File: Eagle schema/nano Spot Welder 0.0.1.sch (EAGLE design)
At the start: 37 parts, among them Q1 BC548, Q3 BD137, T1 BTA 41 / 600V, U1 NANO, U2 DISPLAY-NOKIA-5110, U3 DS18B20, X3 ~230V, X4 Mikro trafó

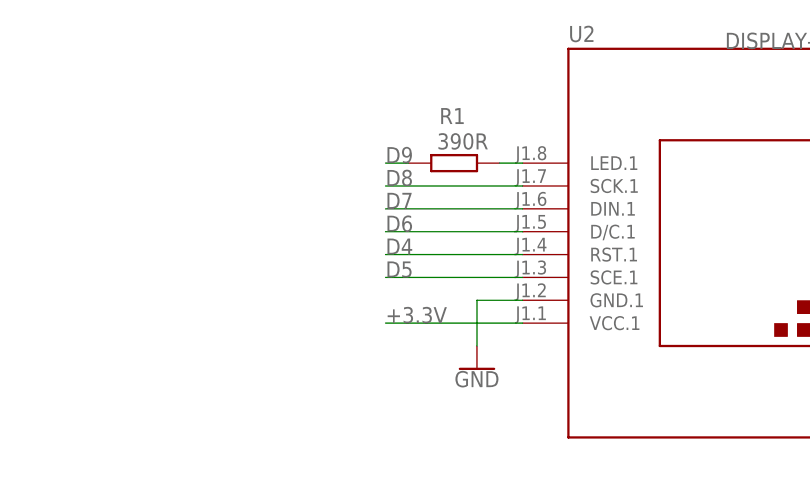
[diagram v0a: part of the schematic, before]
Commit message: - LCD szintillesztő ellenállások - LCD bias & Contrast
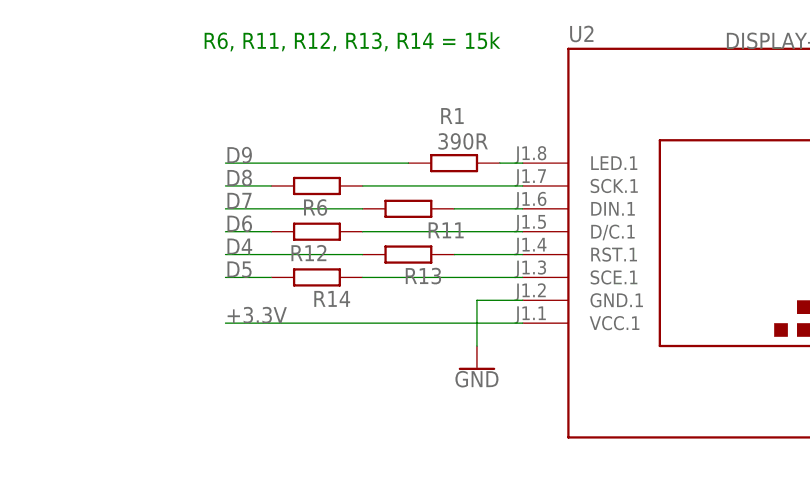
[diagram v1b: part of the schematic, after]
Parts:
- added R11, R12, R13, R14, R6: (no value), resistor:R-EU_0204/7
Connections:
- new net N$10: R12.1, U2.D/C.1
- new net N$11: R13.1, U2.RST.1
- new net N$12: R14.1, U2.SCE.1
- new net N$8: R6.1, U2.SCK.1
- new net N$9: R11.1, U2.DIN.1
- net D4: now also R13.2; no longer U2.RST.1
- net D5: now also R14.2; no longer U2.SCE.1
- net D6: now also R12.2; no longer U2.D/C.1
- net D7: now also R11.2; no longer U2.DIN.1
- net D8: now also R6.2; no longer U2.SCK.1
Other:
- note added: "R6, R11, R12, R13, R14 = 15k"
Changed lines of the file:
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@@
 <layer number="125" name="_tNames" color="7" fill="1" visible="yes" active="yes"/>
 <layer number="126" name="_bNames" color="7" fill="1" visible="yes" active="yes"/>
-<layer number="127" name="_tValues" color="7" fill="1" visible="yes" active="yes"/>
-<layer number="128" name="_bValues" color="7" fill="1" visible="yes" active="yes"/>
+<layer number="127" name="_tValues" color="7" fill="1" visible="no" active="yes"/>
+<layer number="128" name="_bValues" color="7" fill="1" visible="no" active="yes"/>
 <layer number="129" name="Mask" color="7" fill="1" visible="yes" active="yes"/>
 <layer number="130" name="SMDSTROOK" color="7" fill="1" visible="yes" active="yes"/>
@@
 <part name="GND9" library="SparkFun-PowerSymbols" library_urn="urn:adsk.eagle:library:530" deviceset="GND" device=""/>
 <part name="R5" library="resistor" library_urn="urn:adsk.eagle:library:348" deviceset="R-EU_" device="0204/7" package3d_urn="urn:adsk.eagle:package:25945/1" value="56kk"/>
+<part name="R6" library="resistor" library_urn="urn:adsk.eagle:library:348" deviceset="R-EU_" device="0204/7" package3d_urn="urn:adsk.eagle:package:25945/1">
+<attribute name="SPICEPREFIX" value="R"/>
+</part>
+<part name="R11" library="resistor" library_urn="urn:adsk.eagle:library:348" deviceset="R-EU_" device="0204/7" package3d_urn="urn:adsk.eagle:package:25945/1"/>
+<part name="R12" library="resistor" library_urn="urn:adsk.eagle:library:348" deviceset="R-EU_" device="0204/7" package3d_urn="urn:adsk.eagle:package:25945/1"/>
+<part name="R13" library="resistor" library_urn="urn:adsk.eagle:library:348" deviceset="R-EU_" device="0204/7" package3d_urn="urn:adsk.eagle:package:25945/1"/>
+<part name="R14" library="resistor" library_urn="urn:adsk.eagle:library:348" deviceset="R-EU_" device="0204/7" package3d_urn="urn:adsk.eagle:package:25945/1"/>
 </parts>
 <sheets>
@@
 <text x="81.28" y="68.58" size="1.778" layer="91">SW</text>
 <text x="81.28" y="66.04" size="1.778" layer="91">DT</text>
+<text x="50.8" y="129.54" size="1.778" layer="91">R6, R11, R12, R13, R14 = 15k</text>
 </plain>
 <instances>
@@
 <attribute name="NAME" x="1.4986" y="-21.59" size="1.778" layer="95" rot="R270"/>
 <attribute name="VALUE" x="-3.302" y="-21.59" size="1.778" layer="96" rot="R270"/>
+</instance>
+<instance part="R6" gate="G$1" x="63.5" y="114.3" smashed="yes" rot="R180">
+<attribute name="NAME" x="64.77" y="112.8014" size="1.778" layer="95" rot="R180"/>
+<attribute name="VALUE" x="67.31" y="117.602" size="1.778" layer="96" rot="R180"/>
+</instance>
+<instance part="R11" gate="G$1" x="73.66" y="111.76" smashed="yes" rot="R180">
+<attribute name="NAME" x="80.01" y="110.2614" size="1.778" layer="95" rot="R180"/>
+<attribute name="VALUE" x="77.47" y="115.062" size="1.778" layer="96" rot="R180"/>
+</instance>
+<instance part="R12" gate="G$1" x="63.5" y="109.22" smashed="yes" rot="R180">
+<attribute name="NAME" x="64.77" y="107.7214" size="1.778" layer="95" rot="R180"/>
+<attribute name="VALUE" x="67.31" y="112.522" size="1.778" layer="96" rot="R180"/>
+</instance>
+<instance part="R13" gate="G$1" x="73.66" y="106.68" smashed="yes" rot="R180">
+<attribute name="NAME" x="77.47" y="105.1814" size="1.778" layer="95" rot="R180"/>
+<attribute name="VALUE" x="77.47" y="109.982" size="1.778" layer="96" rot="R180"/>
+</instance>
+<instance part="R14" gate="G$1" x="63.5" y="104.14" smashed="yes" rot="R180">
+<attribute name="NAME" x="67.31" y="102.6414" size="1.778" layer="95" rot="R180"/>
+<attribute name="VALUE" x="67.31" y="107.442" size="1.778" layer="96" rot="R180"/>
 </instance>
 </instances>
@@
 <segment>
 <pinref part="U2" gate="G$1" pin="VCC.1"/>
-<wire x1="86.36" y1="99.06" x2="71.12" y2="99.06" width="0.1524" layer="91"/>
-<label x="71.12" y="99.06" size="1.778" layer="95"/>
+<wire x1="86.36" y1="99.06" x2="53.34" y2="99.06" width="0.1524" layer="91"/>
+<label x="53.34" y="99.06" size="1.778" layer="95"/>
 </segment>
 <segment>
@@
 <segment>
 <pinref part="R1" gate="G$1" pin="2"/>
-<wire x1="73.66" y1="116.84" x2="71.12" y2="116.84" width="0.1524" layer="91"/>
-<label x="71.12" y="116.84" size="1.778" layer="95"/>
+<wire x1="73.66" y1="116.84" x2="53.34" y2="116.84" width="0.1524" layer="91"/>
+<label x="53.34" y="116.84" size="1.778" layer="95"/>
 </segment>
 <segment>
@@
 <net name="D4" class="0">
 <segment>
-<pinref part="U2" gate="G$1" pin="RST.1"/>
-<wire x1="86.36" y1="106.68" x2="71.12" y2="106.68" width="0.1524" layer="91"/>
-<label x="71.12" y="106.68" size="1.778" layer="95"/>
-</segment>
-<segment>
 <pinref part="U1" gate="G$1" pin="D4"/>
 <wire x1="-15.24" y1="99.06" x2="-5.08" y2="99.06" width="0.1524" layer="91"/>
 <label x="-7.62" y="99.06" size="1.778" layer="95"/>
 </segment>
+<segment>
+<pinref part="R13" gate="G$1" pin="2"/>
+<wire x1="68.58" y1="106.68" x2="53.34" y2="106.68" width="0.1524" layer="91"/>
+<label x="53.34" y="106.68" size="1.778" layer="95"/>
+</segment>
 </net>
 <net name="D5" class="0">
@@
 </segment>
 <segment>
-<pinref part="U2" gate="G$1" pin="SCE.1"/>
-<wire x1="86.36" y1="104.14" x2="71.12" y2="104.14" width="0.1524" layer="91"/>
-<label x="71.12" y="104.14" size="1.778" layer="95"/>
+<pinref part="R14" gate="G$1" pin="2"/>
+<wire x1="58.42" y1="104.14" x2="53.34" y2="104.14" width="0.1524" layer="91"/>
+<label x="53.34" y="104.14" size="1.778" layer="95"/>
 </segment>
 </net>
@@
 </segment>
 <segment>
-<pinref part="U2" gate="G$1" pin="D/C.1"/>
-<wire x1="86.36" y1="109.22" x2="71.12" y2="109.22" width="0.1524" layer="91"/>
-<label x="71.12" y="109.22" size="1.778" layer="95"/>
+<pinref part="R12" gate="G$1" pin="2"/>
+<wire x1="58.42" y1="109.22" x2="53.34" y2="109.22" width="0.1524" layer="91"/>
+<label x="53.34" y="109.22" size="1.778" layer="95"/>
 </segment>
 </net>
@@
 </segment>
 <segment>
-<pinref part="U2" gate="G$1" pin="DIN.1"/>
-<wire x1="86.36" y1="111.76" x2="71.12" y2="111.76" width="0.1524" layer="91"/>
-<label x="71.12" y="111.76" size="1.778" layer="95"/>
+<pinref part="R11" gate="G$1" pin="2"/>
+<wire x1="68.58" y1="111.76" x2="53.34" y2="111.76" width="0.1524" layer="91"/>
+<label x="53.34" y="111.76" size="1.778" layer="95"/>
 </segment>
 </net>
@@
 </segment>
 <segment>
-<pinref part="U2" gate="G$1" pin="SCK.1"/>
-<wire x1="86.36" y1="114.3" x2="71.12" y2="114.3" width="0.1524" layer="91"/>
-<label x="71.12" y="114.3" size="1.778" layer="95"/>
+<pinref part="R6" gate="G$1" pin="2"/>
+<wire x1="58.42" y1="114.3" x2="53.34" y2="114.3" width="0.1524" layer="91"/>
+<label x="53.34" y="114.3" size="1.778" layer="95"/>
 </segment>
 </net>
@@
 </segment>
 </net>
+<net name="N$8" class="0">
+<segment>
+<pinref part="U2" gate="G$1" pin="SCK.1"/>
+<pinref part="R6" gate="G$1" pin="1"/>
+<wire x1="86.36" y1="114.3" x2="68.58" y2="114.3" width="0.1524" layer="91"/>
+</segment>
+</net>
+<net name="N$9" class="0">
+<segment>
+<pinref part="U2" gate="G$1" pin="DIN.1"/>
+<pinref part="R11" gate="G$1" pin="1"/>
+<wire x1="86.36" y1="111.76" x2="78.74" y2="111.76" width="0.1524" layer="91"/>
+</segment>
+</net>
+<net name="N$10" class="0">
+<segment>
+<pinref part="U2" gate="G$1" pin="D/C.1"/>
+<pinref part="R12" gate="G$1" pin="1"/>
+<wire x1="86.36" y1="109.22" x2="68.58" y2="109.22" width="0.1524" layer="91"/>
+</segment>
+</net>
+<net name="N$11" class="0">
+<segment>
+<pinref part="U2" gate="G$1" pin="RST.1"/>
+<pinref part="R13" gate="G$1" pin="1"/>
+<wire x1="86.36" y1="106.68" x2="78.74" y2="106.68" width="0.1524" layer="91"/>
+</segment>
+</net>
+<net name="N$12" class="0">
+<segment>
+<pinref part="U2" gate="G$1" pin="SCE.1"/>
+<pinref part="R14" gate="G$1" pin="1"/>
+<wire x1="86.36" y1="104.14" x2="68.58" y2="104.14" width="0.1524" layer="91"/>
+</segment>
+</net>

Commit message: - rajzok
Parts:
- removed R11, R12, R13, R14, R6: (no value), resistor:R-EU_0204/7
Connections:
- removed net N$10: R12.1, U2.D/C.1
- removed net N$11: R13.1, U2.RST.1
- removed net N$12: R14.1, U2.SCE.1
- removed net N$8: R6.1, U2.SCK.1
- removed net N$9: R11.1, U2.DIN.1
- net D4: now also U2.RST.1; no longer R13.2
- net D5: now also U2.SCE.1; no longer R14.2
- net D6: now also U2.D/C.1; no longer R12.2
- net D7: now also U2.DIN.1; no longer R11.2
- net D8: now also U2.SCK.1; no longer R6.2
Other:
- note removed: "R6, R11, R12, R13, R14 = 15k"
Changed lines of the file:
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@@
 <part name="GND9" library="SparkFun-PowerSymbols" library_urn="urn:adsk.eagle:library:530" deviceset="GND" device=""/>
 <part name="R5" library="resistor" library_urn="urn:adsk.eagle:library:348" deviceset="R-EU_" device="0204/7" package3d_urn="urn:adsk.eagle:package:25945/1" value="56kk"/>
-<part name="R6" library="resistor" library_urn="urn:adsk.eagle:library:348" deviceset="R-EU_" device="0204/7" package3d_urn="urn:adsk.eagle:package:25945/1">
-<attribute name="SPICEPREFIX" value="R"/>
-</part>
-<part name="R11" library="resistor" library_urn="urn:adsk.eagle:library:348" deviceset="R-EU_" device="0204/7" package3d_urn="urn:adsk.eagle:package:25945/1"/>
-<part name="R12" library="resistor" library_urn="urn:adsk.eagle:library:348" deviceset="R-EU_" device="0204/7" package3d_urn="urn:adsk.eagle:package:25945/1"/>
-<part name="R13" library="resistor" library_urn="urn:adsk.eagle:library:348" deviceset="R-EU_" device="0204/7" package3d_urn="urn:adsk.eagle:package:25945/1"/>
-<part name="R14" library="resistor" library_urn="urn:adsk.eagle:library:348" deviceset="R-EU_" device="0204/7" package3d_urn="urn:adsk.eagle:package:25945/1"/>
 </parts>
 <sheets>
@@
 <text x="81.28" y="68.58" size="1.778" layer="91">SW</text>
 <text x="81.28" y="66.04" size="1.778" layer="91">DT</text>
-<text x="50.8" y="129.54" size="1.778" layer="91">R6, R11, R12, R13, R14 = 15k</text>
 </plain>
 <instances>
@@
 <attribute name="NAME" x="1.4986" y="-21.59" size="1.778" layer="95" rot="R270"/>
 <attribute name="VALUE" x="-3.302" y="-21.59" size="1.778" layer="96" rot="R270"/>
-</instance>
-<instance part="R6" gate="G$1" x="63.5" y="114.3" smashed="yes" rot="R180">
-<attribute name="NAME" x="64.77" y="112.8014" size="1.778" layer="95" rot="R180"/>
-<attribute name="VALUE" x="67.31" y="117.602" size="1.778" layer="96" rot="R180"/>
-</instance>
-<instance part="R11" gate="G$1" x="73.66" y="111.76" smashed="yes" rot="R180">
-<attribute name="NAME" x="80.01" y="110.2614" size="1.778" layer="95" rot="R180"/>
-<attribute name="VALUE" x="77.47" y="115.062" size="1.778" layer="96" rot="R180"/>
-</instance>
-<instance part="R12" gate="G$1" x="63.5" y="109.22" smashed="yes" rot="R180">
-<attribute name="NAME" x="64.77" y="107.7214" size="1.778" layer="95" rot="R180"/>
-<attribute name="VALUE" x="67.31" y="112.522" size="1.778" layer="96" rot="R180"/>
-</instance>
-<instance part="R13" gate="G$1" x="73.66" y="106.68" smashed="yes" rot="R180">
-<attribute name="NAME" x="77.47" y="105.1814" size="1.778" layer="95" rot="R180"/>
-<attribute name="VALUE" x="77.47" y="109.982" size="1.778" layer="96" rot="R180"/>
-</instance>
-<instance part="R14" gate="G$1" x="63.5" y="104.14" smashed="yes" rot="R180">
-<attribute name="NAME" x="67.31" y="102.6414" size="1.778" layer="95" rot="R180"/>
-<attribute name="VALUE" x="67.31" y="107.442" size="1.778" layer="96" rot="R180"/>
 </instance>
 </instances>
@@
 <segment>
 <pinref part="U2" gate="G$1" pin="VCC.1"/>
-<wire x1="86.36" y1="99.06" x2="53.34" y2="99.06" width="0.1524" layer="91"/>
-<label x="53.34" y="99.06" size="1.778" layer="95"/>
+<wire x1="86.36" y1="99.06" x2="66.04" y2="99.06" width="0.1524" layer="91"/>
+<label x="66.04" y="99.06" size="1.778" layer="95"/>
 </segment>
 <segment>
@@
 <segment>
 <pinref part="R1" gate="G$1" pin="2"/>
-<wire x1="73.66" y1="116.84" x2="53.34" y2="116.84" width="0.1524" layer="91"/>
-<label x="53.34" y="116.84" size="1.778" layer="95"/>
+<wire x1="73.66" y1="116.84" x2="66.04" y2="116.84" width="0.1524" layer="91"/>
+<label x="66.04" y="116.84" size="1.778" layer="95"/>
 </segment>
 <segment>
@@
 </segment>
 <segment>
-<pinref part="R13" gate="G$1" pin="2"/>
-<wire x1="68.58" y1="106.68" x2="53.34" y2="106.68" width="0.1524" layer="91"/>
-<label x="53.34" y="106.68" size="1.778" layer="95"/>
+<wire x1="86.36" y1="106.68" x2="66.04" y2="106.68" width="0.1524" layer="91"/>
+<label x="66.04" y="106.68" size="1.778" layer="95"/>
+<pinref part="U2" gate="G$1" pin="RST.1"/>
 </segment>
 </net>
@@
 </segment>
 <segment>
-<pinref part="R14" gate="G$1" pin="2"/>
-<wire x1="58.42" y1="104.14" x2="53.34" y2="104.14" width="0.1524" layer="91"/>
-<label x="53.34" y="104.14" size="1.778" layer="95"/>
+<label x="66.04" y="104.14" size="1.778" layer="95"/>
+<pinref part="U2" gate="G$1" pin="SCE.1"/>
+<wire x1="86.36" y1="104.14" x2="66.04" y2="104.14" width="0.1524" layer="91"/>
 </segment>
 </net>
@@
 </segment>
 <segment>
-<pinref part="R12" gate="G$1" pin="2"/>
-<wire x1="58.42" y1="109.22" x2="53.34" y2="109.22" width="0.1524" layer="91"/>
-<label x="53.34" y="109.22" size="1.778" layer="95"/>
+<label x="66.04" y="109.22" size="1.778" layer="95"/>
+<pinref part="U2" gate="G$1" pin="D/C.1"/>
+<wire x1="86.36" y1="109.22" x2="66.04" y2="109.22" width="0.1524" layer="91"/>
 </segment>
 </net>
@@
 </segment>
 <segment>
-<pinref part="R11" gate="G$1" pin="2"/>
-<wire x1="68.58" y1="111.76" x2="53.34" y2="111.76" width="0.1524" layer="91"/>
-<label x="53.34" y="111.76" size="1.778" layer="95"/>
+<wire x1="86.36" y1="111.76" x2="66.04" y2="111.76" width="0.1524" layer="91"/>
+<label x="66.04" y="111.76" size="1.778" layer="95"/>
+<pinref part="U2" gate="G$1" pin="DIN.1"/>
 </segment>
 </net>
@@
 </segment>
 <segment>
-<pinref part="R6" gate="G$1" pin="2"/>
-<wire x1="58.42" y1="114.3" x2="53.34" y2="114.3" width="0.1524" layer="91"/>
-<label x="53.34" y="114.3" size="1.778" layer="95"/>
+<label x="66.04" y="114.3" size="1.778" layer="95"/>
+<pinref part="U2" gate="G$1" pin="SCK.1"/>
+<wire x1="86.36" y1="114.3" x2="66.04" y2="114.3" width="0.1524" layer="91"/>
 </segment>
 </net>
@@
 </segment>
 </net>
-<net name="N$8" class="0">
-<segment>
-<pinref part="U2" gate="G$1" pin="SCK.1"/>
-<pinref part="R6" gate="G$1" pin="1"/>
-<wire x1="86.36" y1="114.3" x2="68.58" y2="114.3" width="0.1524" layer="91"/>
-</segment>
-</net>
-<net name="N$9" class="0">
-<segment>
-<pinref part="U2" gate="G$1" pin="DIN.1"/>
-<pinref part="R11" gate="G$1" pin="1"/>
-<wire x1="86.36" y1="111.76" x2="78.74" y2="111.76" width="0.1524" layer="91"/>
-</segment>
-</net>
-<net name="N$10" class="0">
-<segment>
-<pinref part="U2" gate="G$1" pin="D/C.1"/>
-<pinref part="R12" gate="G$1" pin="1"/>
-<wire x1="86.36" y1="109.22" x2="68.58" y2="109.22" width="0.1524" layer="91"/>
-</segment>
-</net>
-<net name="N$11" class="0">
-<segment>
-<pinref part="U2" gate="G$1" pin="RST.1"/>
-<pinref part="R13" gate="G$1" pin="1"/>
-<wire x1="86.36" y1="106.68" x2="78.74" y2="106.68" width="0.1524" layer="91"/>
-</segment>
-</net>
-<net name="N$12" class="0">
-<segment>
-<pinref part="U2" gate="G$1" pin="SCE.1"/>
-<pinref part="R14" gate="G$1" pin="1"/>
-<wire x1="86.36" y1="104.14" x2="68.58" y2="104.14" width="0.1524" layer="91"/>
-</segment>
-</net>
